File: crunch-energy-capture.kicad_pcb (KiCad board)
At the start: 2 copper layers, 26 parts, among them U1 EPM1210SJ

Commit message: work in progress
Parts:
- added D14: 600V, Diode_THT:D_DO-201AE_P15.24mm_Horizontal, F.Cu at (22.9, 20.3)
- added H1: MountingHole_Pad, MountingHole:MountingHole_3.5mm_Pad_TopBottom, F.Cu at (63.5, 61.0)
- added H2: MountingHole_Pad, MountingHole:MountingHole_3.5mm_Pad_TopBottom, F.Cu at (214.6, 61.0)
- added H3: MountingHole, MountingHole:MountingHole_3.5mm, F.Cu at (212.1, 138.4)
- added J1: Input, Library:KEYSTONE_7693, F.Cu at (66.0, 105.4)
- added J2: Ground, Library:KEYSTONE_7693, F.Cu at (66.0, 72.4)
- added J3: Bus+, Library:KEYSTONE_7693, F.Cu at (88.9, 38.1)
- added J4: Bus-, Library:KEYSTONE_7693, F.Cu at (88.9, 139.7)
- added J5: Screw_Terminal_01x02, TerminalBlock_MetzConnect:TerminalBlock_MetzConnect_Type011_RT05502HBLC_1x02_P5.00mm_Horizontal, F.Cu at (211.0, 96.6)
- added J6: Screw_Terminal_01x02, TerminalBlock_MetzConnect:TerminalBlock_MetzConnect_Type011_RT05502HBLC_1x02_P5.00mm_Horizontal, F.Cu at (213.5, 40.7)
- added U2: XL-4015-Buck-PCB, Library:XL4015-Buck-Module, F.Cu at (190.6, 62.8)
- C1: value C -> 2.2nF
- D1, D2: footprint Diode_THT:D_DO-201AE_P15.24mm_Horizontal -> Diode_SMD:D_SMC_Handsoldering
- D10, D6, D7, D8, D9: value 75V -> BZT52B75; footprint Diode_THT:D_DO-35_SOD27_P7.62mm_Horizontal -> Diode_SMD:D_SOD-123F
- D11: value 1N5337B -> 1SMB5917; footprint Diode_THT:D_DO-201_P15.24mm_Horizontal -> Diode_SMD:D_SMB_Handsoldering
- D12: value UF5408 -> MURS4100C; footprint Diode_THT:D_DO-201AD_P15.24mm_Horizontal -> Diode_SMD:D_SMC_Handsoldering
- D3, D4: footprint Diode_THT:D_DO-201AE_P15.24mm_Horizontal -> Diode_SMD:D_SMC_Handsoldering; moved to B.Cu
- moved D11 50.6 mm to (81.3, 116.8)
- moved D1 44.1 mm to (77.5, 96.5), turned to 180 degrees
- moved R2 42.0 mm to (76.2, 114.3), turned to 180 degrees
- moved D13 39.6 mm to (74.9, 119.4), turned to 0 degrees
- moved D10 38.4 mm to (88.9, 109.2)
- moved D9 35.6 mm to (88.9, 114.3)
- moved D8 33.4 mm to (88.9, 119.4)
- moved D3 33.0 mm to (77.5, 96.5), turned to 0 degrees
- moved D7 30.5 mm to (88.9, 124.5)
- moved D5 29.3 mm to (80.0, 128.3)
- moved C2 29.0 mm to (78.7, 137.2)
- moved R1 29.0 mm to (78.7, 141.0)
- moved D6 28.4 mm to (88.9, 129.5)
- moved D2 24.7 mm to (77.5, 81.3), turned to 180 degrees
- moved D4 24.7 mm to (77.5, 81.3), turned to 0 degrees
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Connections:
- net Net-(D1-A1) renamed /RECT+
- net Net-(D1-A2) renamed /IN
- net Net-(D12-K) renamed /BUS+
- net Net-(D2-A2) renamed /IN_GND
- net Net-(D3-A2) renamed /BUS-
- net Net-(U1-+DCOUT) renamed /12V+
- net Net-(U1--DCOUT) renamed /12V_GND
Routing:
- net /RECT+: track 0.00 -> 45.6 mm
- added copper zone on F.Cu, net /BUS+
- added copper zone on B.Cu, net /BUS-

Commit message: add GDT
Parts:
- removed D14: 600V, Diode_THT:D_DO-201AE_P15.24mm_Horizontal
- added GD1: 350V, Diode_THT:D_5KP_P10.16mm_Horizontal, F.Cu at (33.9, 41.6)
- D5: value MCR12DSNT4G -> SCR
- moved H2 22.9 mm to (214.6, 38.1)
- moved J6 8.89 mm to (213.5, 49.6)

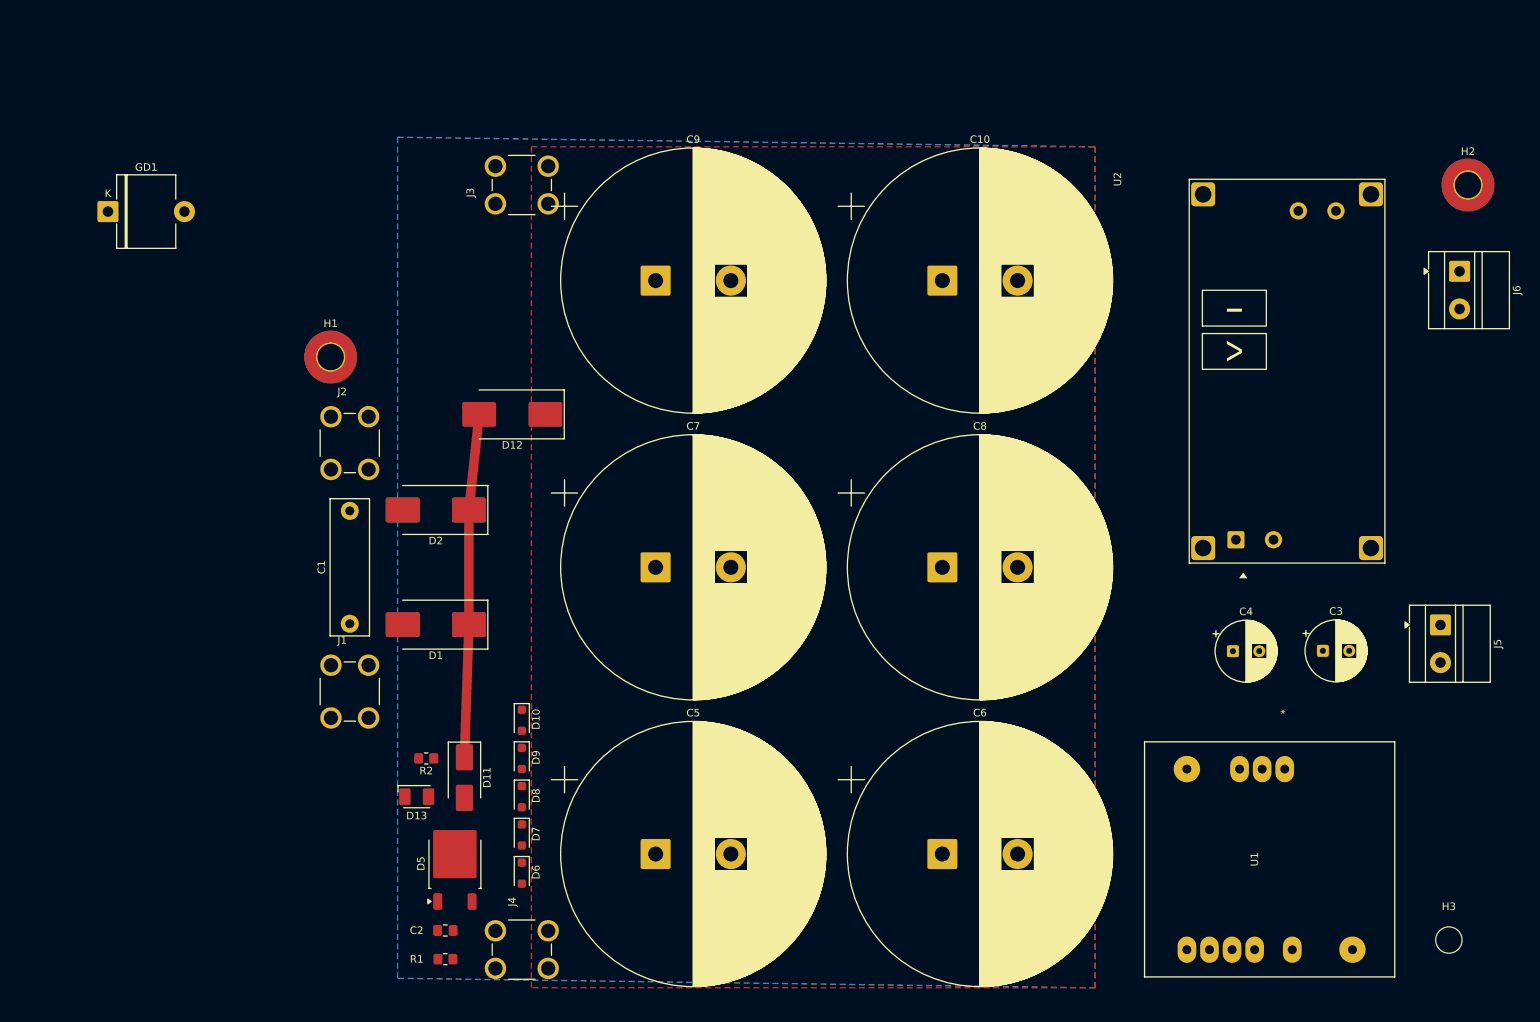
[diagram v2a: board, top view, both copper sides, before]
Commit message: finished layout and ordered
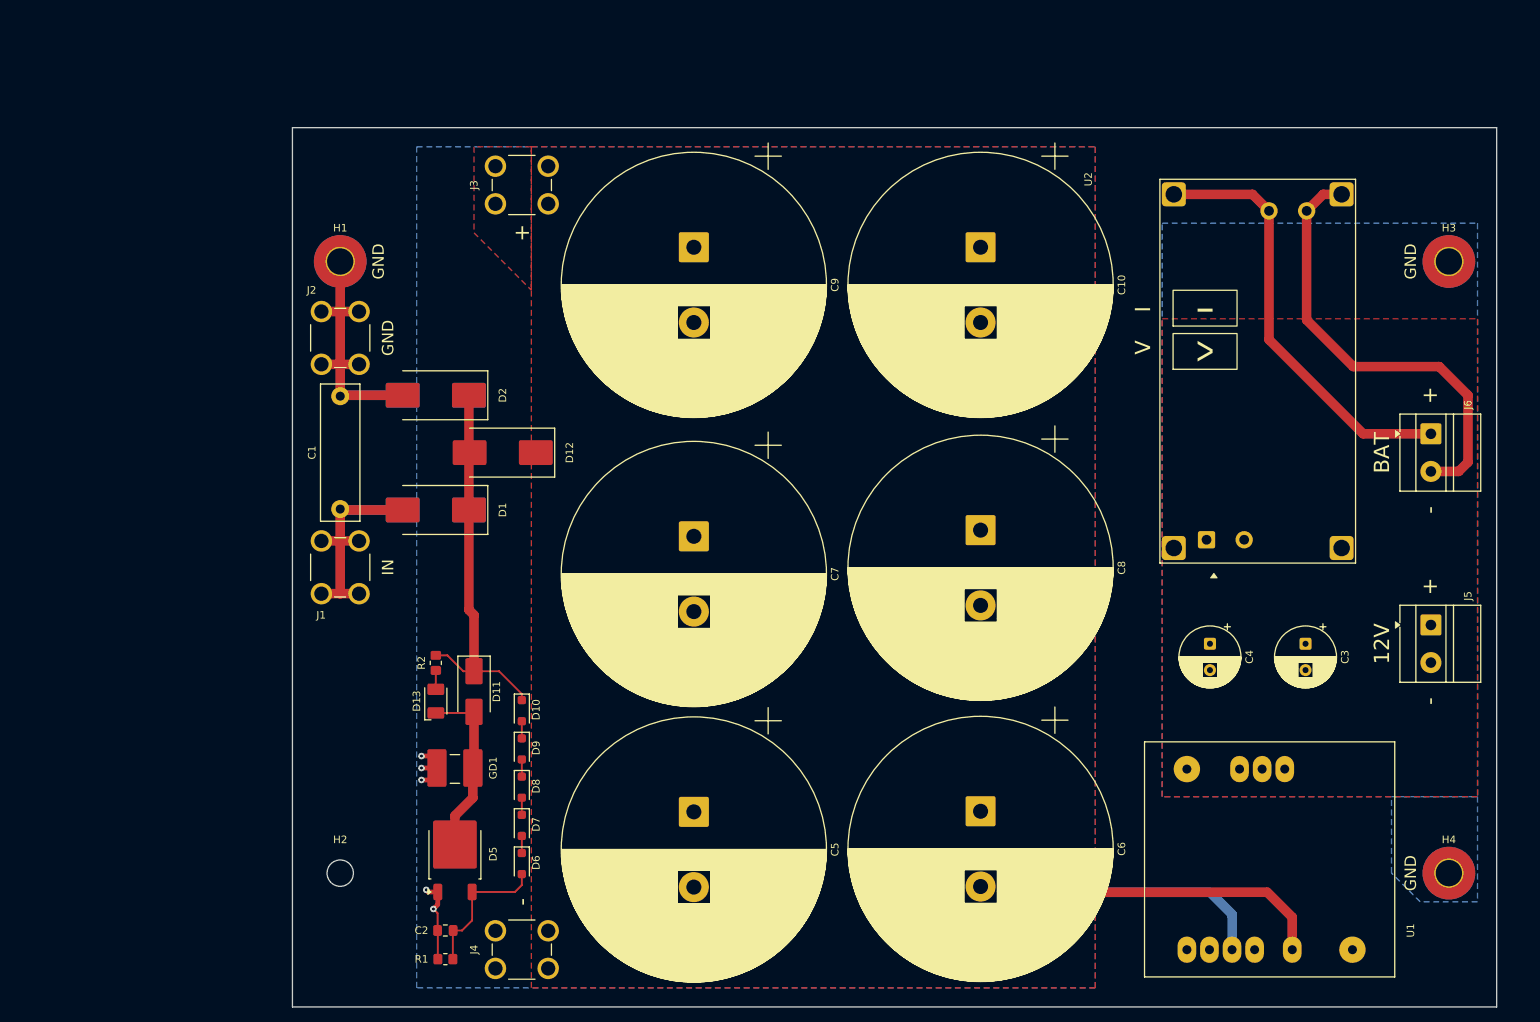
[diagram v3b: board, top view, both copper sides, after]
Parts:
- removed the H3 at (212.1, 138.4)
- added H2: MountingHole, MountingHole:MountingHole_3.5mm, F.Cu at (64.8, 129.5)
- added H4: MountingHole_Pad, MountingHole:MountingHole_3.5mm_Pad_TopBottom, F.Cu at (212.1, 129.5)
- GD1: footprint Diode_THT:D_5KP_P10.16mm_Horizontal -> Library:GDT_Bourns_2053_SM
- moved GD1 87.1 mm to (80.0, 115.6)
- moved J6 21.9 mm to (209.7, 71.2)
- moved J1 16.6 mm to (64.8, 88.9)
- moved C1 15.3 mm to (64.8, 81.2)
- moved D1 15.2 mm to (77.5, 81.3)
- moved D2 15.2 mm to (77.5, 66.0)
- moved D3 15.2 mm to (77.5, 81.3)
- moved D4 15.2 mm to (77.5, 66.0)
- moved J2 14.0 mm to (64.8, 58.4)
- moved D13 13.0 mm to (77.5, 106.7), turned to 90 degrees
- moved H1 12.8 mm to (64.8, 48.3)
- moved R2 12.8 mm to (77.5, 101.6), turned to -90 degrees
- moved D11 11.5 mm to (82.5, 105.4)
- moved H3 10.5 mm to (212.1, 48.3)
- moved C6 7.62 mm to (149.9, 121.3), turned to -90 degrees
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- renumbered H2 to H3
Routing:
- net /BAT-: track 0.00 -> 60.0 mm
- net /BAT+: track 0.00 -> 57.4 mm
- net /BUS-: track 0.00 -> 46.9 mm, vias 0 -> 5
- net /IN_GND: track 0.00 -> 44.6 mm
- net /IN: track 0.00 -> 37.9 mm
- net /BUS+: track 0.00 -> 34.4 mm
- net Net-(D11-A): track 0.00 -> 23.8 mm
- net Net-(D5-G): track 0.00 -> 19.1 mm
- net /RECT+: track 45.6 -> 51.4 mm
- net Net-(D13-A): track 0.00 -> 2.51 mm
- net Net-(D7-K): track 0.00 -> 2.28 mm
- net Net-(D6-K): track 0.00 -> 2.28 mm
- net Net-(D10-A): track 0.00 -> 2.28 mm
- net Net-(D8-K): track 0.00 -> 2.28 mm
- added copper zone on F.Cu, net /12V+
- added copper zone on B.Cu, net /12V_GND
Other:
- board outline added: 160 x 116.8 mm
- board text added: "+"
- board text added: "-"
- board text added: "12V"
- board text added: "BAT"
- board text added: "GND"
- board text added: "I"
- board text added: "IN"
- board text added: "V"
